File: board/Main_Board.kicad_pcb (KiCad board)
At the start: 2 copper layers, 61.5 x 34.8 mm, 19 parts, among them J2 Encoder J2 Encoder, J3 Encoder J3 Encoder, J4 Encoder J4 Encoder, U1 Teensy4.1_DEV-16771

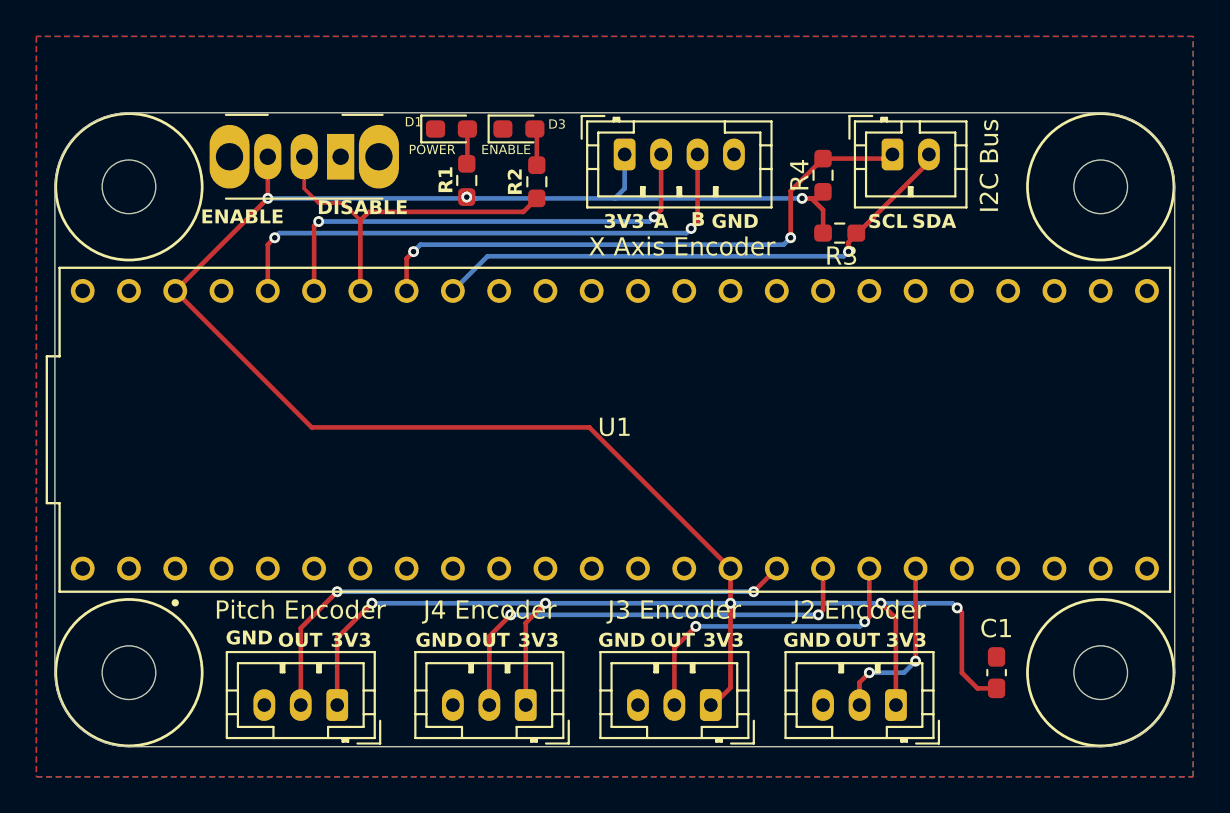
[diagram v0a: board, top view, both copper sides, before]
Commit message: Adjust LED positions - fix DRC error
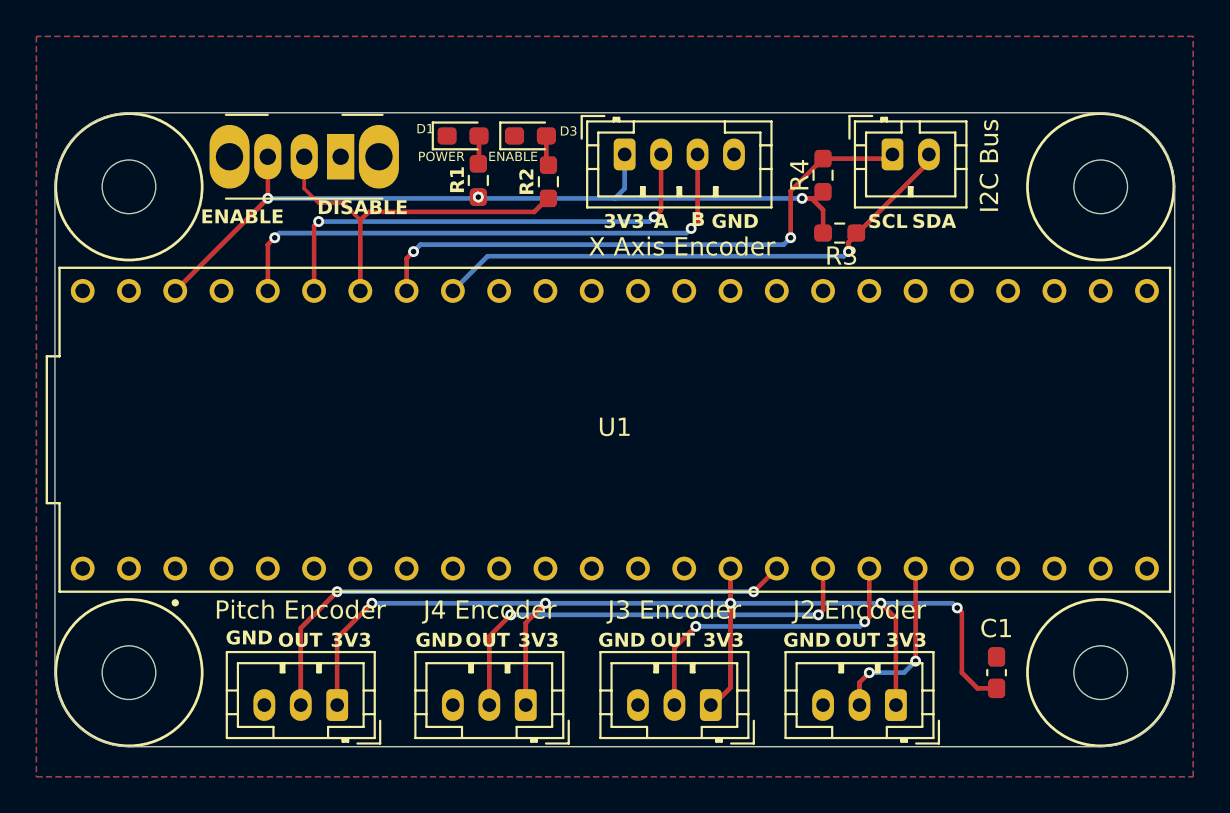
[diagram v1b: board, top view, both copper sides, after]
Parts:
- moved D3 0.74 mm to (141.4, 69.0)
- moved D1 0.74 mm to (137.7, 69.0)
- moved R1 0.63 mm to (138.6, 71.4)
- moved R2 0.63 mm to (142.4, 71.5)
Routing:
- net +3V3: track 147.8 -> 110.8 mm
- net Enable: track 20.3 -> 20.9 mm
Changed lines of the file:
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@@
 	(footprint "LED_SMD:LED_0603_1608Metric_Pad1.05x0.95mm_HandSolder"
 		(layer "F.Cu")
-		(at 140.784 68.58)
+		(at 141.419 68.961)
 		(descr "LED SMD 0603 (1608 Metric), square (rectangular) end terminal, IPC-7351 nominal, (Body size source: http://www.tortai-tech.com/upload/download/2011102023233369053.pdf), generated with kicad-footprint-generator")
 		(tags "LED handsolder")
@@
 	(footprint "Resistor_SMD:R_0603_1608Metric_Pad0.98x0.95mm_HandSolder"
 		(layer "F.Cu")
-		(at 137.922 71.406 90)
+		(at 138.557 71.406 90)
 		(descr "Resistor SMD 0603 (1608 Metric), square (rectangular) end terminal, IPC-7351 nominal with elongated pad for handsoldering. (Body size source: IPC-SM-782 page 72, https://www.pcb-3d.com/wordpress/wp-content/uploads/ipc-sm-782a_amendment_1_and_2.pdf), generated with kicad-footprint-generator")
 		(tags "resistor handsolder")
@@
 	(footprint "LED_SMD:LED_0603_1608Metric_Pad1.05x0.95mm_HandSolder"
 		(layer "F.Cu")
-		(at 137.083 68.58)
+		(at 137.718 68.961)
 		(descr "LED SMD 0603 (1608 Metric), square (rectangular) end terminal, IPC-7351 nominal, (Body size source: http://www.tortai-tech.com/upload/download/2011102023233369053.pdf), generated with kicad-footprint-generator")
 		(tags "LED handsolder")
@@
 	(footprint "Resistor_SMD:R_0603_1608Metric_Pad0.98x0.95mm_HandSolder"
 		(layer "F.Cu")
-		(at 141.768 71.4775 90)
+		(at 142.403 71.4775 90)
 		(descr "Resistor SMD 0603 (1608 Metric), square (rectangular) end terminal, IPC-7351 nominal with elongated pad for handsoldering. (Body size source: IPC-SM-782 page 72, https://www.pcb-3d.com/wordpress/wp-content/uploads/ipc-sm-782a_amendment_1_and_2.pdf), generated with kicad-footprint-generator")
 		(tags "resistor handsolder")
@@
 	)
 	(gr_text "ENABLE"
-		(at 140.081 69.723 0)
+		(at 140.462 70.104 0)
 		(layer "F.SilkS")
 		(effects
@@
 	)
 	(gr_text "POWER"
-		(at 136.017 69.723 0)
+		(at 136.525 70.104 0)
 		(layer "F.SilkS")
 		(effects
@@
 	)
 	(segment
-		(start 144.653 84.963)
-		(end 129.413 84.963)
-		(width 0.254)
-		(layer "F.Cu")
-		(net 4)
-	)
-	(segment
 		(start 165.1 98.425)
 		(end 165.9625 99.2875)
@@
 	)
 	(segment
-		(start 152.4 92.71)
-		(end 144.653 84.963)
-		(width 0.254)
-		(layer "F.Cu")
-		(net 4)
-	)
-	(segment
-		(start 129.413 84.963)
-		(end 121.92 77.47)
-		(width 0.254)
-		(layer "F.Cu")
-		(net 4)
-	)
-	(segment
 		(start 156.845 72.39)
 		(end 157.48 73.025)
@@
 	)
 	(via
-		(at 137.922 72.3185)
+		(at 138.557 72.3185)
 		(size 0.6)
 		(drill 0.3)
@@
 	(segment
 		(start 138.43 72.39)
-		(end 146.05 72.39)
+		(end 138.684 72.39)
 		(width 0.254)
 		(layer "B.Cu")
@@
 	)
 	(segment
-		(start 138.43 72.39)
-		(end 137.9935 72.39)
-		(width 0.254)
-		(layer "B.Cu")
-		(net 4)
-	)
-	(segment
 		(start 146.59 69.85)
 		(end 146.59 71.85)
@@
 	)
 	(segment
+		(start 138.6125 72.3185)
+		(end 138.684 72.39)
+		(width 0.254)
+		(layer "B.Cu")
+		(net 4)
+	)
+	(segment
 		(start 164.592 94.615)
 		(end 160.655 94.615)
@@
 	)
 	(segment
-		(start 137.9935 72.39)
-		(end 137.922 72.3185)
+		(start 138.557 72.3185)
+		(end 138.4855 72.39)
+		(width 0.254)
+		(layer "B.Cu")
+		(net 4)
+	)
+	(segment
+		(start 138.684 72.39)
+		(end 146.05 72.39)
+		(width 0.254)
+		(layer "B.Cu")
+		(net 4)
+	)
+	(segment
+		(start 138.557 72.3185)
+		(end 138.6125 72.3185)
+		(width 0.254)
+		(layer "B.Cu")
+		(net 4)
+	)
+	(segment
+		(start 138.4855 72.39)
+		(end 138.43 72.39)
 		(width 0.254)
 		(layer "B.Cu")
@@
 	)
 	(segment
-		(start 137.958 68.58)
-		(end 137.958 70.565)
+		(start 138.593 68.961)
+		(end 138.593 70.4575)
+		(width 0.254)
+		(layer "F.Cu")
+		(net 10)
+	)
+	(segment
+		(start 138.593 70.4575)
+		(end 138.557 70.4935)
 		(width 0.254)
 		(layer "F.Cu")
@@
 	)
 	(segment
-		(start 141.024 73.134)
-		(end 141.768 72.39)
-		(width 0.254)
+		(start 129 71.85)
+		(end 129.794 72.644)
+		(width 0.2)
 		(layer "F.Cu")
 		(net 46)
 	)
 	(segment
-		(start 129 71.85)
-		(end 129.794 72.644)
-		(width 0.2)
+		(start 141.623 73.134)
+		(end 142.367 72.39)
+		(width 0.254)
 		(layer "F.Cu")
 		(net 46)
@@
 	)
 	(segment
+		(start 142.367 72.39)
+		(end 142.403 72.39)
+		(width 0.254)
+		(layer "F.Cu")
+		(net 46)
+	)
+	(segment
 		(start 132.532 73.134)
-		(end 141.024 73.134)
+		(end 141.623 73.134)
 		(width 0.254)
 		(layer "F.Cu")
@@
 	)
 	(segment
-		(start 141.768 70.565)
-		(end 141.768 68.689)
+		(start 142.294 68.961)
+		(end 142.294 70.456)
 		(width 0.254)
 		(layer "F.Cu")
@@
 	)
 	(segment
-		(start 141.768 68.689)
-		(end 141.659 68.58)
+		(start 142.294 70.456)
+		(end 142.403 70.565)
 		(width 0.254)
 		(layer "F.Cu")

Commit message: Add signatures & ground vias
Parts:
- added G***: LOGO, LOGO, B.Cu at (123.5, 81.9)
- added G***: LOGO, LOGO, B.Cu at (124.0, 87.1)
- added sign: LOGO, LOGO, B.Cu at (35.7, 21.9)
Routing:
- net GND: vias 0 -> 10

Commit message: Clean up before order
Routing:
- net +3V3: track 110.8 -> 135.6 mm
- net SDA: track 29.9 -> 34.9 mm
- net AE4: track 31.8 -> 33.1 mm
- net SCL: track 32.4 -> 33.3 mm
- net AE2: track 17.3 -> 18.0 mm
- net AE3: track 25.1 -> 25.8 mm
- net AE1: track 10.0 -> 10.7 mm
- net QE1-A: track 26.1 -> 26.7 mm
- net QE1-B: track 30.5 -> 30.9 mm, vias 2 -> 1
